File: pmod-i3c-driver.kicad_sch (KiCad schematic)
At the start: 77 parts, among them J1 PinSocket_2x12_P2.54mm_Drill1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, J2 PinSocket_2x6_P2.54mm_Drill1.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, J3 JST_SH_1x4_SM04B-SRSS-TB-LF-SN, J4 USB-C_CUI_UJC-HP-3-SMT-TR, J5 PinHeader_1x3_P2.54mm_Drill1.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, J6 PinHeader_1x3_P2.54mm_Drill1.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, J7 PinHeader_2x10_P1.27mm_SMD, Q1 DMC31D5UDJ, Q2 DMC31D5UDJ, Q3 DMC2400UV-7, Q4 DMC2400UV-7, Q5 DMG1012T-7, U1 TPS7A0518P_SOT23-5, U2 SN74LVC1G240_SC70, U3 SN74LVC1G240_SC70, U4 TLV70033_SC70

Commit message: Update naming convention
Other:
- title: I3C output stage adapter -> I3C output stage

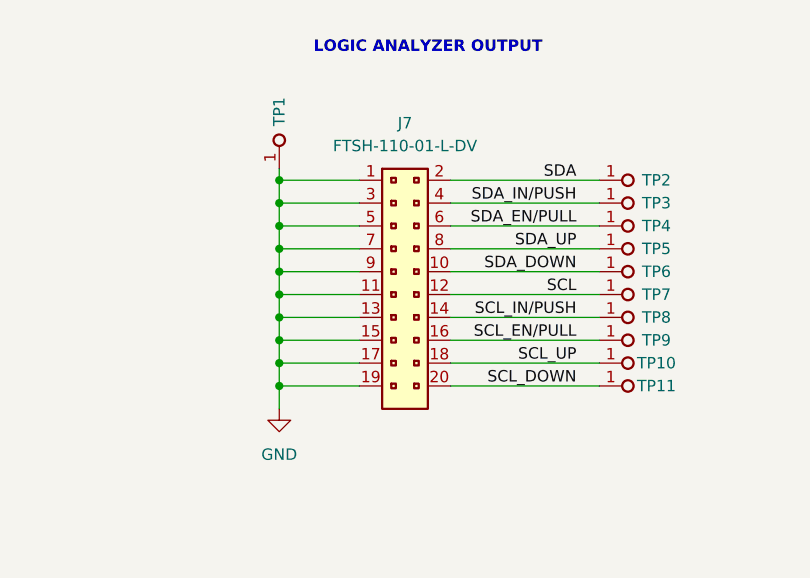
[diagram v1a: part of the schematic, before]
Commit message: Make J7 DNP
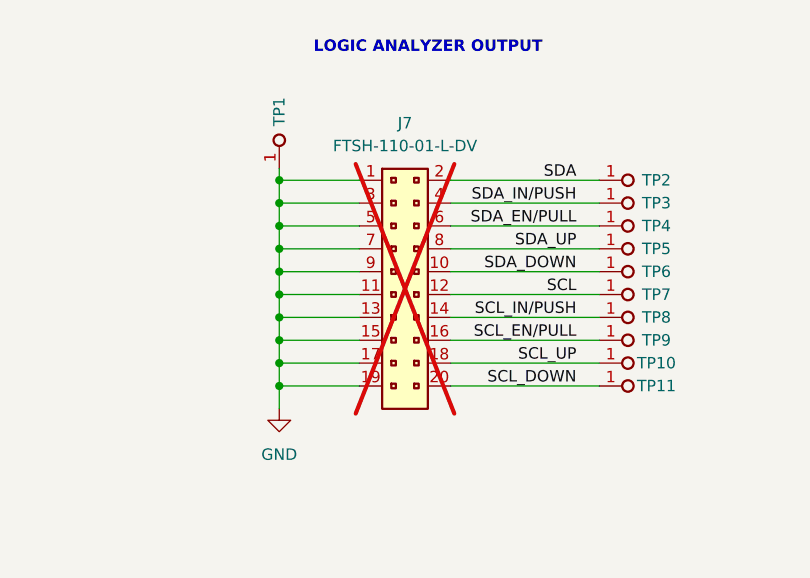
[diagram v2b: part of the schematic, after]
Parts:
- J7: now not fitted; now left out of the parts list
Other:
- title: I3C output stage -> PMOD I3C Driver
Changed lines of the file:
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@@
   (paper "A3")
   (title_block
-    (title "I3C output stage")
+    (title "PMOD I3C Driver")
     (date "2024-11-05")
     (rev "1.0.0")
@@
   )
   (symbol (lib_id "antmicroGenericPinHeaders:PinHeader_2x10_P1.27mm_SMD") (at 345.44 176.53 0) (unit 1)
-    (in_bom yes) (on_board yes) (dnp no) (fields_autoplaced)
+    (in_bom no) (on_board no) (dnp yes) (fields_autoplaced)
     (property "Reference" "J7" (at 350.52 170.18 0)
       (effects (font (size 1.27 1.27) (thickness 0.15)))
